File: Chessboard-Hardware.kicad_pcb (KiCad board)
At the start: 2 copper layers, 100 x 100 mm, 19 parts, among them IC1 SS49E, IC10 SS49E, IC11 SS49E, IC12 SS49E, IC13 SS49E, IC14 SS49E, IC15 SS49E, IC16 SS49E, IC2 SS49E, IC3 SS49E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

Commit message: Layout SSe49s
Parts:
- moved IC11 103.7 mm to (112.5, 116.2)
- moved IC12 101.5 mm to (137.5, 116.2)
- moved IC16 100.9 mm to (137.5, 141.2)
- moved IC13 100.1 mm to (62.5, 141.2)
- moved IC7 99.8 mm to (112.5, 91.2)
- moved U1 99.8 mm to (185.5, 108.0)
- moved C1 99.8 mm to (181.1, 118.5)
- moved J1 99.8 mm to (159.8, 101.8)
- moved IC15 98.8 mm to (112.5, 141.2)
- moved IC1 97.9 mm to (62.5, 66.2)
- moved IC8 97.7 mm to (137.5, 91.2)
- moved IC14 96.8 mm to (87.5, 141.2)
- moved IC2 96.4 mm to (87.5, 66.2)
- moved IC5 95.8 mm to (62.5, 91.2)
- moved IC9 95.5 mm to (62.5, 116.2)
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
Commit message: PCB
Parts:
- moved U1 85.9 mm to (100.0, 99.8), turned to -90 degrees
- moved C1 70.1 mm to (111.8, 107.6), turned to 180 degrees
- moved J1 51.2 mm to (148.2, 51.8)
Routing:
- net VCC: track 0.00 -> 461.4 mm, vias 0 -> 5
- net GND: track 0.00 -> 447.6 mm, vias 0 -> 3
- net Net-(J1-Pin_3): track 0.00 -> 82.4 mm, vias 0 -> 1
- net Net-(J1-Pin_7): track 0.00 -> 79.0 mm
- net Net-(J1-Pin_5): track 0.00 -> 71.7 mm, vias 0 -> 2
- net Net-(J1-Pin_8): track 0.00 -> 71.0 mm, vias 0 -> 1
- net Net-(J1-Pin_6): track 0.00 -> 70.4 mm, vias 0 -> 2
- net Net-(IC16-O): track 0.00 -> 62.3 mm, vias 0 -> 1
- net Net-(J1-Pin_4): track 0.00 -> 56.1 mm, vias 0 -> 1
- net Net-(IC13-O): track 0.00 -> 53.5 mm, vias 0 -> 1
- net Net-(IC1-O): track 0.00 -> 52.6 mm
- net Net-(IC4-O): track 0.00 -> 51.5 mm
- net Net-(IC9-O): track 0.00 -> 50.9 mm
- net Net-(IC12-O): track 0.00 -> 44.6 mm
- net Net-(IC15-O): track 0.00 -> 43.2 mm, vias 0 -> 1
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- added copper zone on B.Cu, net GND
- added copper zone on F.Cu, net VCC

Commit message: PCB done
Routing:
- net VCC: track 461.4 -> 514.6 mm, vias 5 -> 3
- net GND: track 447.6 -> 500.7 mm, vias 3 -> 2
- net Net-(J1-Pin_8): track 71.0 -> 70.0 mm
- removed copper zone on F.Cu, net VCC
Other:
- board text added: "COM"
- board text added: "EN"
- board text added: "GND"
- board text added: "Linear hall 4x4 grid with CD74HC4067M for chessboard"
- board text added: "S0"
- board text added: "S1"
- board text added: "S2"
- board text added: "S3"
- board text added: "VCC"
- board text added: "VCC GND SIG Flat side down"

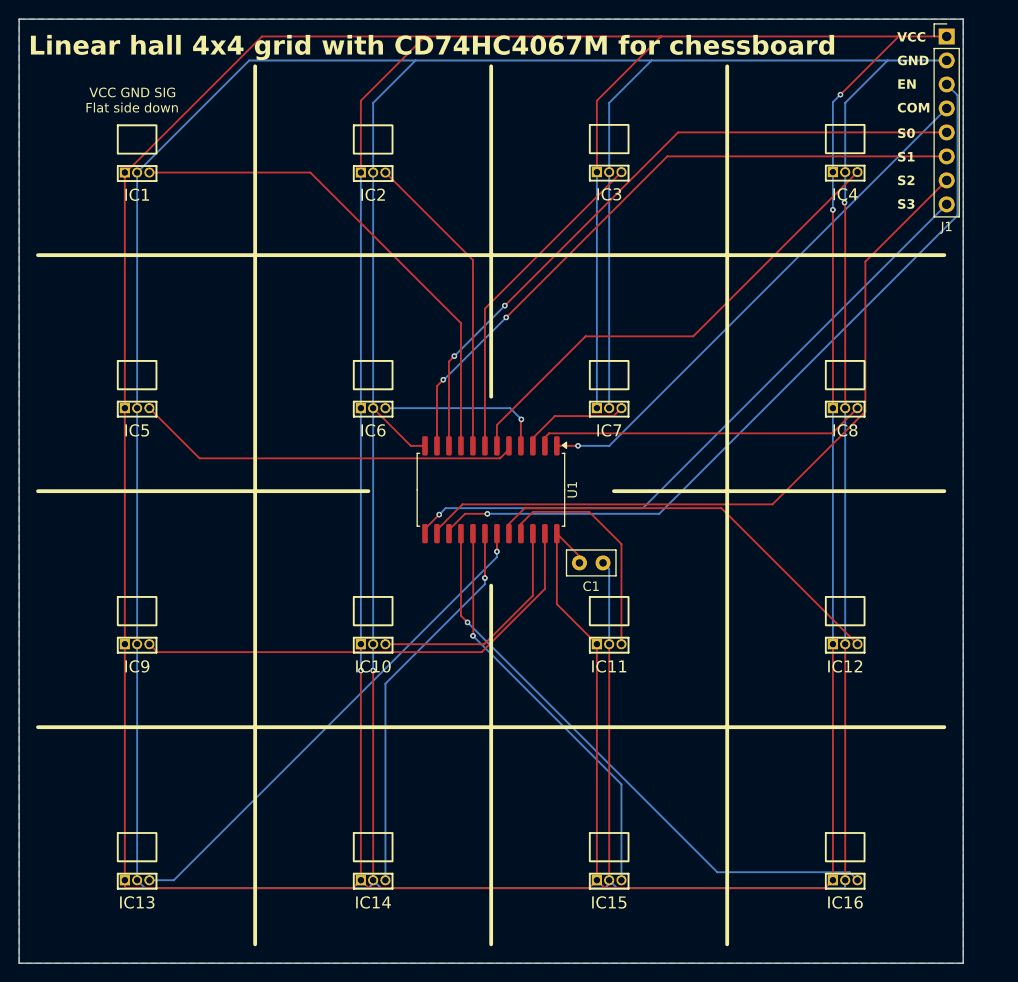
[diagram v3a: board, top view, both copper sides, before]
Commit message: VCC plane
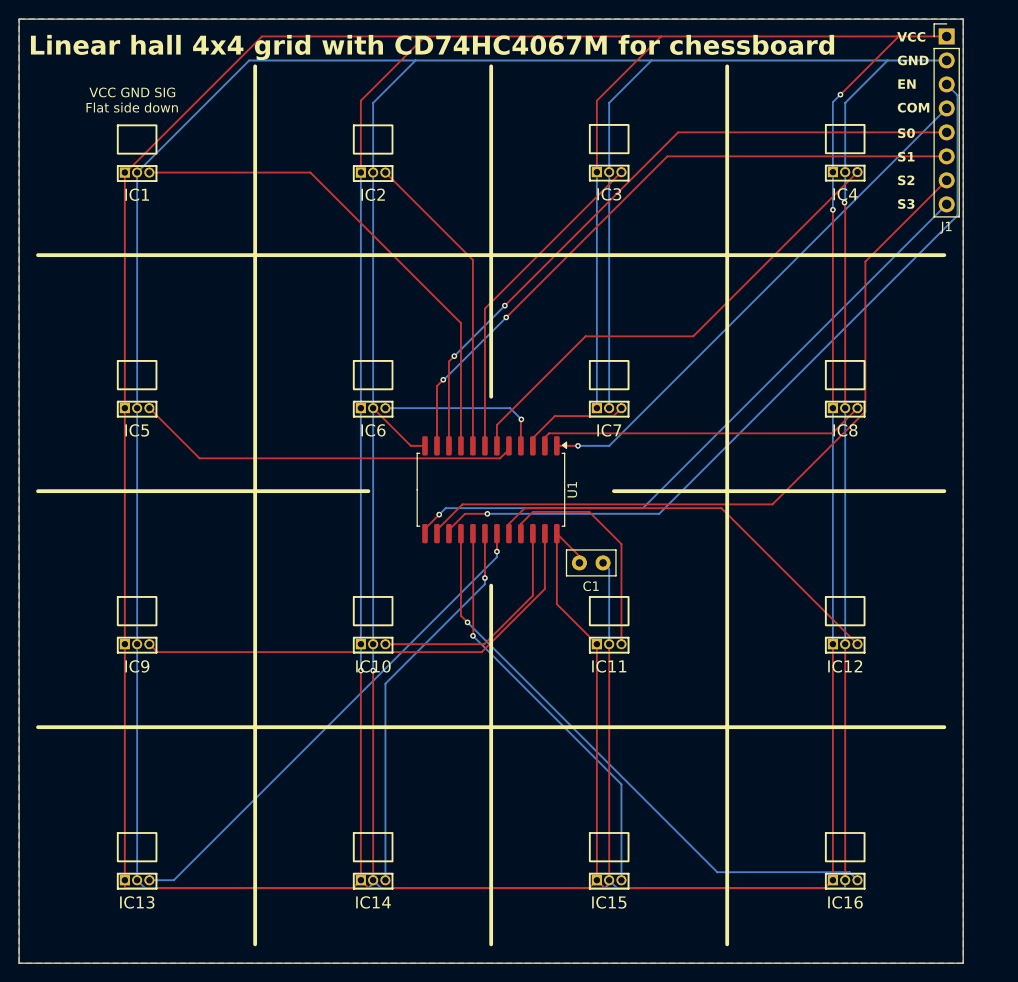
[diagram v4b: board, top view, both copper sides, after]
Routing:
- added copper zone on F.Cu, net VCC
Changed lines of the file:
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@@
+	)
+	(zone
+		(net 2)
+		(net_name "VCC")
+		(layer "F.Cu")
+		(hatch edge 0.5)
+		(priority 1)
+		(connect_pads
+			(clearance 0.5)
+		)
+		(min_thickness 0.25)
+		(filled_areas_thickness no)
+		(fill yes
+			(thermal_gap 0.5)
+			(thermal_bridge_width 0.5)
+		)
+		(polygon
+			(pts
+				(xy 50 50) (xy 150 50) (xy 150 150) (xy 50 150)
+			)
+		)
 	)
 	(zone

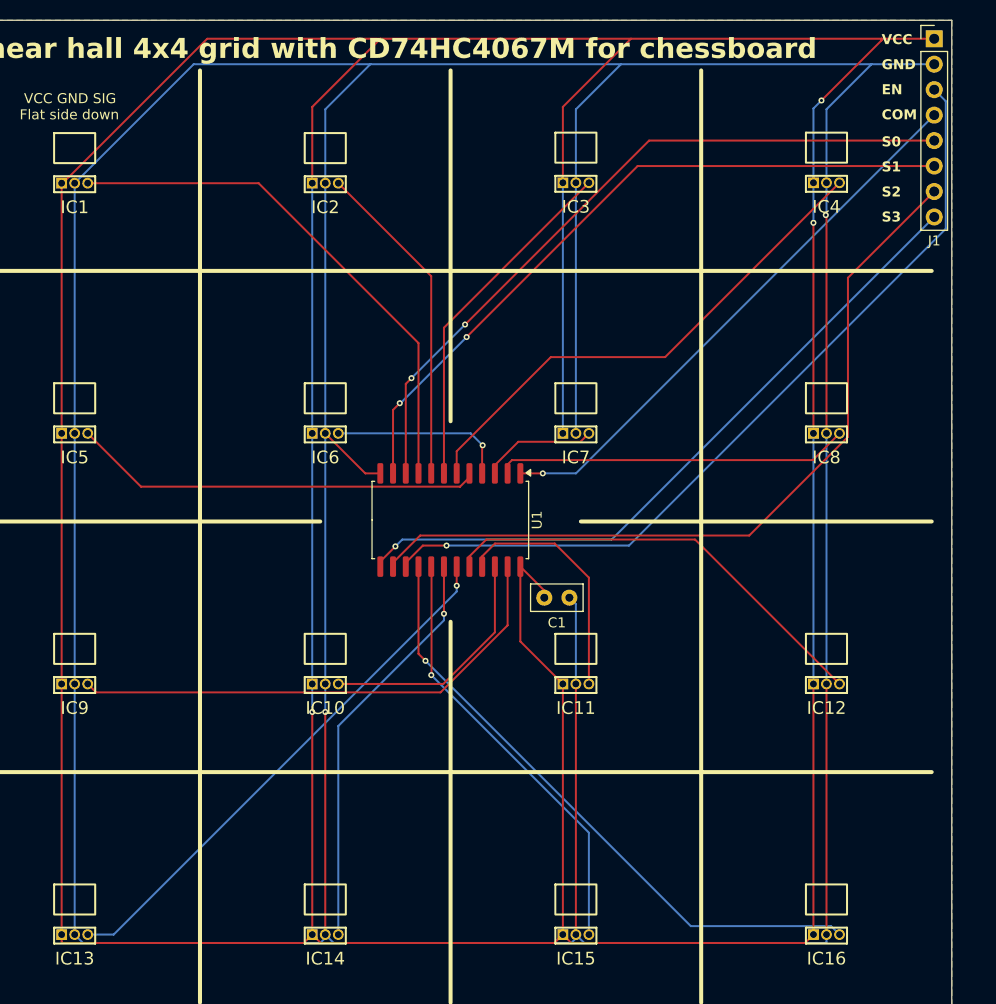
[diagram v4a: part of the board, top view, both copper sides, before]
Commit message: Widen power traces
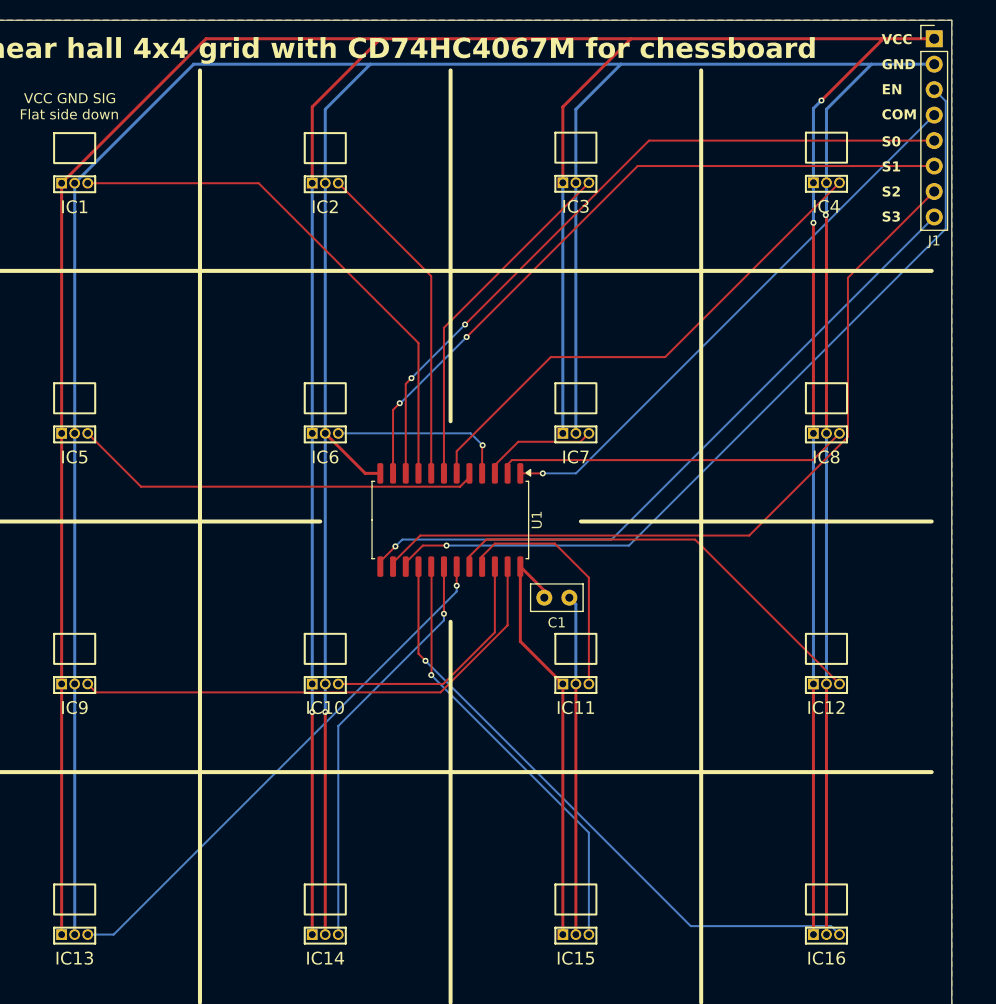
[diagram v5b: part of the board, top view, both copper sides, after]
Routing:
- net GND: track 500.7 -> 422.8 mm
- net VCC: track 514.6 -> 437.1 mm

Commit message: I forgot what I did
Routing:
- net Net-(IC16-O): track 62.3 -> 63.0 mm
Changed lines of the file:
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@@
-	)
-	(segment
-		(start 137.5 141.2075)
-		(end 137.5 116.2075)
-		(width 0.3)
-		(layer "F.Cu")
-		(net 1)
 	)
 	(segment
@@
 		(end 87.5 116.2075)
 		(width 0.3)
+		(layer "B.Cu")
+		(net 1)
+	)
+	(segment
+		(start 137.5 141.2075)
+		(end 137.5 116.2075)
+		(width 0.2)
 		(layer "B.Cu")
 		(net 1)
@@
 	)
 	(segment
-		(start 123.9675 140.3675)
-		(end 137.96 140.3675)
+		(start 137.96 142.0475)
+		(end 138.8 141.2075)
 		(width 0.2)
 		(layer "B.Cu")
@@
 	)
 	(segment
+		(start 125.6475 142.0475)
+		(end 137.96 142.0475)
+		(width 0.2)
+		(layer "B.Cu")
+		(net 18)
+	)
+	(segment
 		(start 97.5 113.9)
-		(end 123.9675 140.3675)
-		(width 0.2)
-		(layer "B.Cu")
-		(net 18)
-	)
-	(segment
-		(start 137.96 140.3675)
-		(end 138.8 141.2075)
-		(width 0.2)
-		(layer "B.Cu")
+		(end 125.6475 142.0475)
+		(width 0.2)
+		(layer "B.Cu")
